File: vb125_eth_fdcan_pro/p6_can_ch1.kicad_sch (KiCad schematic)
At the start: 35 parts, among them J6 D09P33E4GL00LF, K1 EE2-4.5TNUH, M2 B0505MT-1WR4, Q1 BSS138, U7 ADM3050EBRIZ, U8 TLP2270

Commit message: Add variants.
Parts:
- C1, C2, C36, C65, C66, D12, D5, FB3, FB4, J6, K1, L3, M2, Q1, R19, U7, U8: Variant (none) -> can_ch2
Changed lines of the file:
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@@
+      (effects (font (size 1.27 1.27)) hide)
+    )
+    (property "Variant" "can_ch2" (at 189.23 69.85 0)
       (effects (font (size 1.27 1.27)) hide)
     )
@@
       (effects (font (size 1.27 1.27)) hide)
     )
+    (property "Variant" "can_ch2" (at 107.95 114.3 0)
+      (effects (font (size 1.27 1.27)) hide)
+    )
     (pin "1")
     (pin "2")
@@
     )
     (property "Sim.Pins" "1=K 2=A" (at 275.59 157.48 0)
+      (effects (font (size 1.27 1.27)) hide)
+    )
+    (property "Variant" "can_ch2" (at 275.59 157.48 0)
       (effects (font (size 1.27 1.27)) hide)
     )
@@
     )
     (property "Datasheet" "https://www.analog.com/media/en/technical-documentation/data-sheets/ADM3050E.pdf" (at 191.77 129.54 0)
+      (effects (font (size 1.27 1.27)) hide)
+    )
+    (property "Variant" "can_ch2" (at 180.34 111.76 0)
       (effects (font (size 1.27 1.27)) hide)
     )
@@
       (effects (font (size 1.27 1.27)) (justify left) hide)
     )
+    (property "Variant" "can_ch2" (at 189.23 173.99 0)
+      (effects (font (size 1.27 1.27)) hide)
+    )
     (pin "1")
     (pin "2")
@@
       (effects (font (size 1.27 1.27)) hide)
     )
+    (property "Variant" "can_ch2" (at 289.56 123.19 0)
+      (effects (font (size 1.27 1.27)) hide)
+    )
     (pin "1")
     (pin "2")
@@
     )
     (property "Vworking" "8.7V" (at 138.43 81.28 0)
+      (effects (font (size 1.27 1.27)) hide)
+    )
+    (property "Variant" "can_ch2" (at 138.43 81.28 0)
       (effects (font (size 1.27 1.27)) hide)
     )
@@
       (effects (font (size 1.27 1.27)) hide)
     )
+    (property "Variant" "can_ch2" (at 208.28 190.5 0)
+      (effects (font (size 1.27 1.27)) hide)
+    )
     (pin "1")
     (pin "2")
@@
     )
     (property "Mpn2" "Murata:GRM21BR71A106KA73K" (at 220.98 80.01 0)
+      (effects (font (size 1.27 1.27)) hide)
+    )
+    (property "Variant" "can_ch2" (at 220.98 80.01 0)
       (effects (font (size 1.27 1.27)) hide)
     )
@@
       (effects (font (size 1.27 1.27)) hide)
     )
+    (property "Variant" "can_ch2" (at 165.1 171.45 0)
+      (effects (font (size 1.27 1.27)) hide)
+    )
     (pin "1")
     (pin "2")
@@
       (effects (font (size 1.27 1.27)) hide)
     )
+    (property "Variant" "can_ch2" (at 189.23 226.06 0)
+      (effects (font (size 1.27 1.27)) hide)
+    )
     (pin "1")
     (pin "2")
@@
     )
     (property "Mpn2" "Murata:GRM21BR71A106KA73K" (at 240.03 120.65 0)
+      (effects (font (size 1.27 1.27)) hide)
+    )
+    (property "Variant" "can_ch2" (at 240.03 120.65 0)
       (effects (font (size 1.27 1.27)) hide)
     )
@@
       (effects (font (size 1.27 1.27)) hide)
     )
+    (property "Variant" "can_ch2" (at 147.32 72.39 0)
+      (effects (font (size 1.27 1.27)) hide)
+    )
     (pin "1")
     (pin "2")
@@
       (effects (font (size 1.27 1.27)) hide)
     )
+    (property "Variant" "can_ch2" (at 189.23 220.98 0)
+      (effects (font (size 1.27 1.27)) hide)
+    )
     (pin "1")
     (pin "2")
@@
       (effects (font (size 1.27 1.27)) hide)
     )
+    (property "Variant" "can_ch2" (at 143.51 121.92 0)
+      (effects (font (size 1.27 1.27)) hide)
+    )
     (pin "1")
     (pin "2")
@@
       (effects (font (size 1.27 1.27)) (justify left) hide)
     )
+    (property "Variant" "can_ch2" (at 224.79 173.99 0)
+      (effects (font (size 1.27 1.27)) hide)
+    )
     (pin "1")
     (pin "2")
@@
       (effects (font (size 1.27 1.27)) hide)
     )
+    (property "Variant" "can_ch2" (at 251.46 173.99 0)
+      (effects (font (size 1.27 1.27)) hide)
+    )
     (pin "1")
     (pin "2")
@@
     )
     (property "Vworking" "3.3V" (at 132.08 121.92 0)
+      (effects (font (size 1.27 1.27)) hide)
+    )
+    (property "Variant" "can_ch2" (at 132.08 121.92 0)
       (effects (font (size 1.27 1.27)) hide)
     )
@@
       (effects (font (size 1.27 1.27)) hide)
     )
+    (property "Variant" "can_ch2" (at 227.33 120.65 0)
+      (effects (font (size 1.27 1.27)) hide)
+    )
     (pin "1")
     (pin "2")
@@
       (effects (font (size 1.27 1.27)) (justify left))
     )
+    (property "Variant" "can_ch2" (at 95.25 121.92 0)
+      (effects (font (size 1.27 1.27)) hide)
+    )
     (pin "1")
     (pin "2")
@@
     )
     (property "Datasheet" "https://content.kemet.com/datasheets/KEM_R7002_EC2_EE2.pdf" (at 251.46 157.48 0)
+      (effects (font (size 1.27 1.27)) hide)
+    )
+    (property "Variant" "can_ch2" (at 251.46 157.48 0)
       (effects (font (size 1.27 1.27)) hide)
     )
@@
       (effects (font (size 1.27 1.27)) hide)
     )
+    (property "Variant" "can_ch2" (at 248.92 143.51 0)
+      (effects (font (size 1.27 1.27)) hide)
+    )
     (pin "1")
     (pin "2")
@@
     )
     (property "Datasheet" " ~" (at 326.39 120.65 0)
+      (effects (font (size 1.27 1.27)) hide)
+    )
+    (property "Variant" "can_ch2" (at 326.39 120.65 0)
       (effects (font (size 1.27 1.27)) hide)
     )
@@
       (effects (font (size 1.27 1.27)) (justify left) hide)
     )
+    (property "Variant" "can_ch2" (at 273.05 173.99 0)
+      (effects (font (size 1.27 1.27)) hide)
+    )
     (pin "1")
     (pin "2")
@@
       (effects (font (size 1.27 1.27)) hide)
     )
+    (property "Variant" "can_ch2" (at 227.33 157.48 0)
+      (effects (font (size 1.27 1.27)) hide)
+    )
     (pin "1")
     (pin "2")
@@
       (effects (font (size 1.27 1.27)) hide)
     )
+    (property "Variant" "can_ch2" (at 156.21 81.28 0)
+      (effects (font (size 1.27 1.27)) hide)
+    )
     (pin "1")
     (pin "2")
@@
       (effects (font (size 1.27 1.27)) hide)
     )
+    (property "Variant" "can_ch2" (at 165.1 181.61 0)
+      (effects (font (size 1.27 1.27)) hide)
+    )
     (pin "1")
     (pin "2")
@@
       (effects (font (size 1.27 1.27)) hide)
     )
+    (property "Variant" "can_ch2" (at 119.38 121.92 0)
+      (effects (font (size 1.27 1.27)) hide)
+    )
     (pin "1")
     (pin "2")
@@
       (effects (font (size 1.27 1.27)) hide)
     )
+    (property "Variant" "can_ch2" (at 259.08 143.51 0)
+      (effects (font (size 1.27 1.27)) hide)
+    )
     (pin "1")
     (pin "2")
@@
       (effects (font (size 1.27 1.27)) hide)
     )
+    (property "Variant" "can_ch2" (at 237.49 72.39 0)
+      (effects (font (size 1.27 1.27)) hide)
+    )
     (pin "1")
     (pin "2")
@@
       (effects (font (size 1.27 1.27)) hide)
     )
+    (property "Variant" "can_ch2" (at 214.63 120.65 0)
+      (effects (font (size 1.27 1.27)) hide)
+    )

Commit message: Selection of capacitors for VB125
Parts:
- C1: Mpn1 (none) -> Murata:GRM188Z71C475KE21J; Mpn2 (none) -> Murata:GRM188Z71C475KE21D
- C2: Mpn1 (none) -> Samsung:CL05B104KQ5NNNC; Mpn2 (none) -> YAGEO:CC0402KRX7R5BB104
- C2: Mpn1 (none) -> 0402YC103KAT2A; Mpn2 (none) -> CL05B103KO5NNNC
- C36: Mpn1 (none) -> GRM155R71H472KA01J; Mpn2 (none) -> CC0402KRX7R9BB472
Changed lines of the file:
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@@
+      (effects (font (size 1.27 1.27)) hide)
+    )
+    (property "Mpn1" "Murata:GRM188Z71C475KE21J" (at 138.43 81.28 0)
+      (effects (font (size 1.27 1.27)) hide)
+    )
+    (property "Mpn2" "Murata:GRM188Z71C475KE21D" (at 138.43 81.28 0)
       (effects (font (size 1.27 1.27)) hide)
     )
@@
     )
     (property "Variant" "can_ch2" (at 208.28 190.5 0)
+      (effects (font (size 1.27 1.27)) hide)
+    )
+    (property "Mpn1" "Samsung:CL05B104KQ5NNNC  " (at 208.28 190.5 0)
+      (effects (font (size 1.27 1.27)) hide)
+    )
+    (property "Mpn2" "YAGEO:CC0402KRX7R5BB104" (at 208.28 190.5 0)
       (effects (font (size 1.27 1.27)) hide)
     )
@@
       (effects (font (size 1.27 1.27)) hide)
     )
+    (property "Mpn1" "0402YC103KAT2A" (at 143.51 121.92 0)
+      (effects (font (size 1.27 1.27)) hide)
+    )
+    (property "Mpn2" "CL05B103KO5NNNC" (at 143.51 121.92 0)
+      (effects (font (size 1.27 1.27)) hide)
+    )
     (pin "1")
     (pin "2")
@@
       (effects (font (size 1.27 1.27)) hide)
     )
+    (property "Mpn1" "GRM155R71H472KA01J" (at 251.46 173.99 0)
+      (effects (font (size 1.27 1.27)) hide)
+    )
+    (property "Mpn2" "CC0402KRX7R9BB472" (at 251.46 173.99 0)
+      (effects (font (size 1.27 1.27)) hide)
+    )
     (pin "1")
     (pin "2")
@@
     )
     (property "Variant" "can_ch2" (at 132.08 121.92 0)
+      (effects (font (size 1.27 1.27)) hide)
+    )
+    (property "Mpn1" "Samsung:CL05B104KQ5NNNC  " (at 132.08 121.92 0)
+      (effects (font (size 1.27 1.27)) hide)
+    )
+    (property "Mpn2" "YAGEO:CC0402KRX7R5BB104" (at 132.08 121.92 0)
       (effects (font (size 1.27 1.27)) hide)
     )
@@
     )
     (property "Variant" "can_ch2" (at 227.33 120.65 0)
+      (effects (font (size 1.27 1.27)) hide)
+    )
+    (property "Mpn1" "Samsung:CL05B104KQ5NNNC  " (at 227.33 120.65 0)
+      (effects (font (size 1.27 1.27)) hide)
+    )
+    (property "Mpn2" "YAGEO:CC0402KRX7R5BB104" (at 227.33 120.65 0)
       (effects (font (size 1.27 1.27)) hide)
     )
@@
       (effects (font (size 1.27 1.27)) hide)
     )
+    (property "Mpn1" "Murata:GRM188Z71C475KE21J" (at 156.21 81.28 0)
+      (effects (font (size 1.27 1.27)) hide)
+    )
+    (property "Mpn2" "Murata:GRM188Z71C475KE21D" (at 156.21 81.28 0)
+      (effects (font (size 1.27 1.27)) hide)
+    )
     (pin "1")
     (pin "2")
@@
       (effects (font (size 1.27 1.27)) hide)
     )
+    (property "Mpn1" "0402YC103KAT2A" (at 214.63 120.65 0)
+      (effects (font (size 1.27 1.27)) hide)
+    )
+    (property "Mpn2" "CL05B103KO5NNNC" (at 214.63 120.65 0)
+      (effects (font (size 1.27 1.27)) hide)
+    )

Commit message: Add missing footprints, ready to layout.
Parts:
- D5: footprint (none) -> vhrd_passive_diode:DFN1110D-3_3-XDFN
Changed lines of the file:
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@@
       (effects (font (size 1.27 1.27)))
     )
-    (property "Footprint" "" (at 285.75 123.19 0)
+    (property "Footprint" "vhrd_passive_diode:DFN1110D-3_3-XDFN" (at 285.75 123.19 0)
       (effects (font (size 1.27 1.27)) hide)
     )
-    (property "Datasheet" "~" (at 285.75 123.19 0)
+    (property "Datasheet" "https://assets.nexperia.com/documents/data-sheet/PESD2CANFD24V-QB.pdf" (at 285.75 123.19 0)
       (effects (font (size 1.27 1.27)) hide)
     )

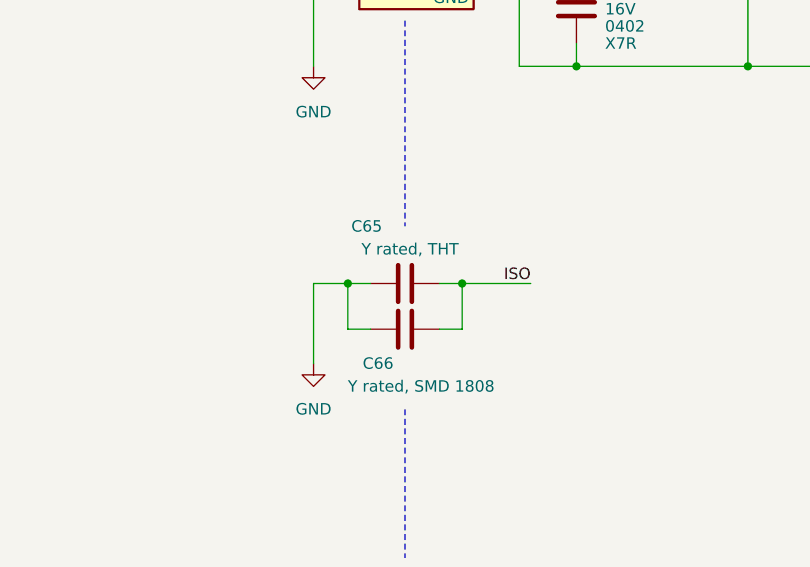
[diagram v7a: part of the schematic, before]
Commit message: Preliminary placement.
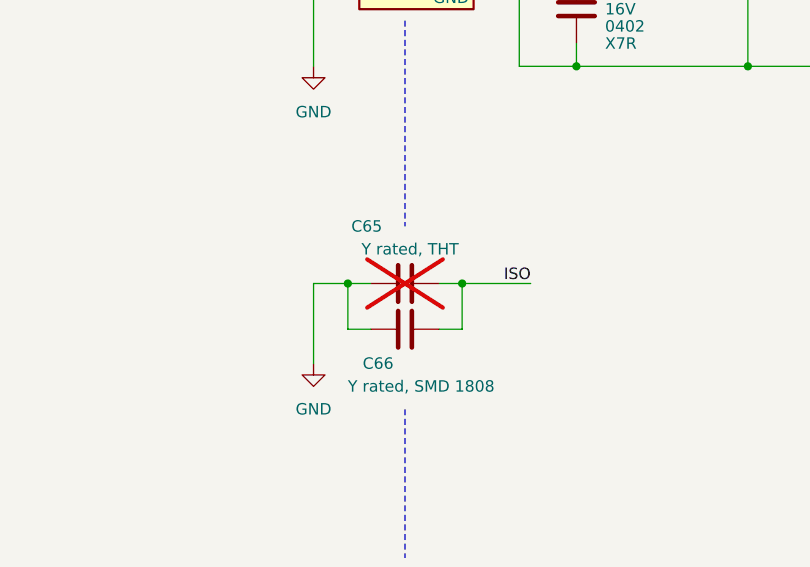
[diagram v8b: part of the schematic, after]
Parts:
- C65: now not fitted; now left out of the parts list
- K1: footprint Relay_SMD:Relay_DPDT_Kemet_EE2_NUH_DoubleCoil -> vhrd_relay:Relay_DPDT_Kemet_EE2_NUH_DoubleCoil
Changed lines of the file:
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@@
   )
   (symbol (lib_id "Device:C") (at 189.23 220.98 90) (unit 1)
-    (in_bom yes) (on_board yes) (dnp no) (fields_autoplaced)
+    (in_bom no) (on_board yes) (dnp yes) (fields_autoplaced)
     (property "Reference" "C65" (at 183.2621 214.63 90)
       (effects (font (size 1.27 1.27)) (justify right))
@@
       (effects (font (size 1.27 1.27)))
     )
-    (property "Footprint" "Relay_SMD:Relay_DPDT_Kemet_EE2_NUH_DoubleCoil" (at 251.46 157.48 0)
-      (effects (font (size 1.27 1.27)) hide)
-    )
+    (property "Footprint" "vhrd_relay:Relay_DPDT_Kemet_EE2_NUH_DoubleCoil" (at 251.46 157.48 0)
+      (effects (font (size 1.27 1.27)) hide)
+    )
